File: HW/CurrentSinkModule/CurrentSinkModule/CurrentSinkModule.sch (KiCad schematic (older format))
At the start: 22 parts

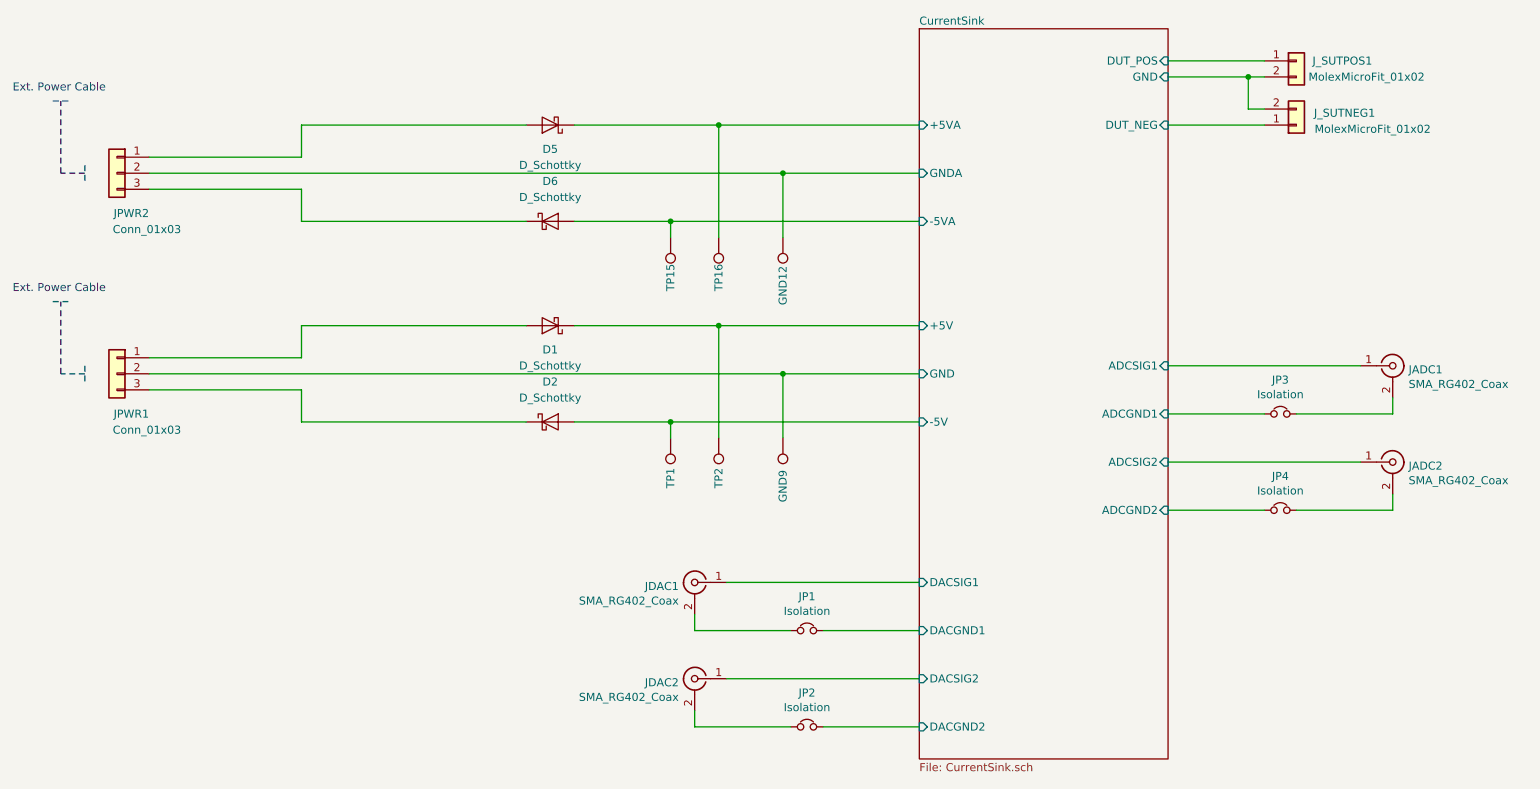
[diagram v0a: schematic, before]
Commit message: Finished CurrentSinkRevC layout
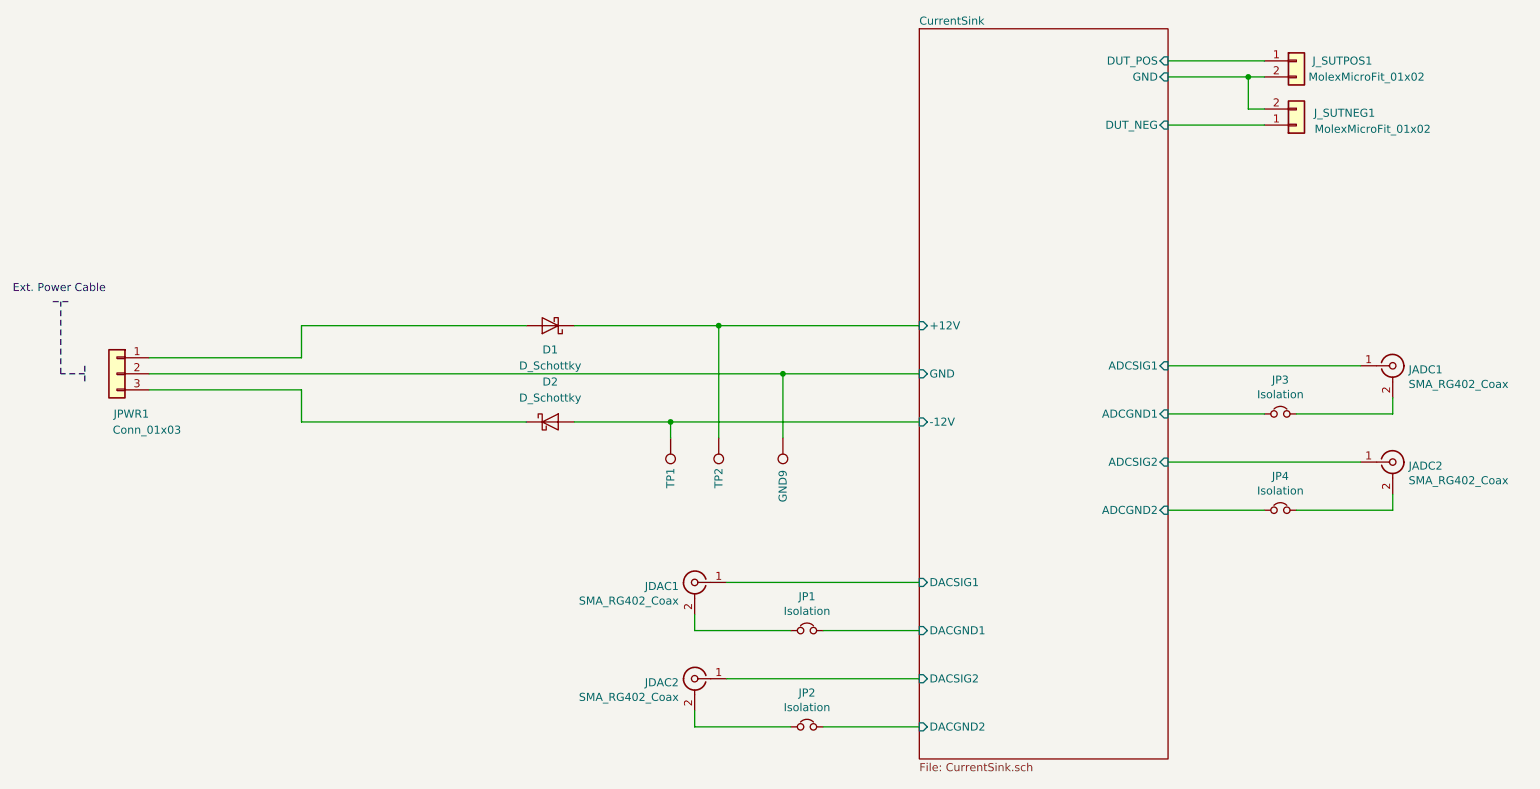
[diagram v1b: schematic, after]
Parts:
- removed D5, D6: D_Schottky, Diode_SMD:D_SOD-123, symbol Device:D_Schottky
- removed GND12, TP15, TP16: TestPoint, TestPoint:TestPoint_Pad_2.0x2.0mm, symbol Connector:TestPoint
- removed JPWR2: Conn_01x03, Connector_Molex:Molex_KK-254_AE-6410-03A_1x03_P2.54mm_Vertical, symbol Connector_Generic:Conn_01x03
- JP1, JP2, JP3, JP4: footprint Jumper:SolderJumper-2_P1.3mm_Bridged_Pad1.0x1.5mm -> Jumper:SolderJumper-2_P1.3mm_Open_Pad1.0x1.5mm
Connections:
- net CurrentSink/GND is gone; now on net CurrentSink/GND: J_SUTNEG1.2 (Pin_2), J_SUTPOS1.2 (Pin_2)
- net CurrentSink/GND: no longer GND9.1, JPWR1.2 (Pin_2)
- net CurrentSink/+5V renamed CurrentSink/+12V
- net CurrentSink/-5V renamed CurrentSink/-12V
- new net CurrentSink/GND: GND9.1, JPWR1.2 (Pin_2)
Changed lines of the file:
@@
 F 0 "JP1" H 5950 5562 50  0000 C CNN
 F 1 "Isolation" H 5950 5471 50  0000 C CNN
-F 2 "Jumper:SolderJumper-2_P1.3mm_Bridged_Pad1.0x1.5mm" H 5950 5350 50  0001 C CNN
+F 2 "Jumper:SolderJumper-2_P1.3mm_Open_Pad1.0x1.5mm" H 5950 5350 50  0001 C CNN
 F 3 "~" H 5950 5350 50  0001 C CNN
 	1    5950 5350
@@
 F 0 "JP2" H 5950 6162 50  0000 C CNN
 F 1 "Isolation" H 5950 6071 50  0000 C CNN
-F 2 "Jumper:SolderJumper-2_P1.3mm_Bridged_Pad1.0x1.5mm" H 5950 5950 50  0001 C CNN
+F 2 "Jumper:SolderJumper-2_P1.3mm_Open_Pad1.0x1.5mm" H 5950 5950 50  0001 C CNN
 F 3 "~" H 5950 5950 50  0001 C CNN
 	1    5950 5950
@@
 F 0 "JP3" H 8900 4212 50  0000 C CNN
 F 1 "Isolation" H 8900 4121 50  0000 C CNN
-F 2 "Jumper:SolderJumper-2_P1.3mm_Bridged_Pad1.0x1.5mm" H 8900 4000 50  0001 C CNN
+F 2 "Jumper:SolderJumper-2_P1.3mm_Open_Pad1.0x1.5mm" H 8900 4000 50  0001 C CNN
 F 3 "~" H 8900 4000 50  0001 C CNN
 	1    8900 4000
@@
 F 0 "JP4" H 8900 4812 50  0000 C CNN
 F 1 "Isolation" H 8900 4721 50  0000 C CNN
-F 2 "Jumper:SolderJumper-2_P1.3mm_Bridged_Pad1.0x1.5mm" H 8900 4600 50  0001 C CNN
+F 2 "Jumper:SolderJumper-2_P1.3mm_Open_Pad1.0x1.5mm" H 8900 4600 50  0001 C CNN
 F 3 "~" H 8900 4600 50  0001 C CNN
 	1    8900 4600
@@
 F12 "DACGND1" I L 6650 5350 50
 F13 "DACGND2" I L 6650 5950 50
-F14 "+5V" I L 6650 3450 50
-F15 "-5V" I L 6650 4050 50
-F16 "+5VA" I L 6650 2200 50
-F17 "-5VA" I L 6650 2800 50
-F18 "GNDA" I L 6650 2500 50
+F14 "+12V" I L 6650 3450 50
+F15 "-12V" I L 6650 4050 50
 $EndSheet
-Wire Wire Line
-	2800 2200 2800 2400
-$Comp
-L Connector_Generic:Conn_01x03 JPWR2
-U 1 1 5E00E9C0
-P 1650 2500
-F 0 "JPWR2" H 1450 2250 50  0000 L CNN
-F 1 "Conn_01x03" H 1250 2150 50  0000 L CNN
-F 2 "Connector_Molex:Molex_KK-254_AE-6410-03A_1x03_P2.54mm_Vertical" H 1650 2500 50  0001 C CNN
-F 3 "~" H 1650 2500 50  0001 C CNN
-	1    1650 2500
-	-1   0    0    -1
-$EndComp
-Wire Notes Line
-	1450 2500 1300 2500
-Wire Notes Line
-	1300 2500 1300 2050
-Wire Notes Line
-	1250 2050 1350 2050
-Wire Notes Line
-	1450 2450 1450 2550
-Text Notes 1000 2000 0    50   ~ 0
-Ext. Power Cable
-$Comp
-L Device:D_Schottky D5
-U 1 1 5E00E9CF
-P 4350 2200
-F 0 "D5" H 4350 2350 50  0000 C CNN
-F 1 "D_Schottky" H 4350 2450 50  0000 C CNN
-F 2 "Diode_SMD:D_SOD-123" H 4350 2200 50  0001 C CNN
-F 3 "~" H 4350 2200 50  0001 C CNN
-	1    4350 2200
-	-1   0    0    1
-$EndComp
-$Comp
-L Device:D_Schottky D6
-U 1 1 5E00E9D9
-P 4350 2800
-F 0 "D6" H 4350 3050 50  0000 C CNN
-F 1 "D_Schottky" H 4350 2950 50  0000 C CNN
-F 2 "Diode_SMD:D_SOD-123" H 4350 2800 50  0001 C CNN
-F 3 "~" H 4350 2800 50  0001 C CNN
-	1    4350 2800
-	1    0    0    -1
-$EndComp
-Wire Wire Line
-	4200 2200 2800 2200
-Wire Wire Line
-	4500 2800 5100 2800
-Wire Wire Line
-	4500 2200 5400 2200
-Wire Wire Line
-	5100 2900 5100 2800
-$Comp
-L Connector:TestPoint TP?
-U 1 1 5E00E9EA
-P 5100 2900
-AR Path="/5C977310/5E00E9EA" Ref="TP?"  Part="1"
-AR Path="/5E00E9EA" Ref="TP15"  Part="1"
-F 0 "TP15" V 5100 3150 50  0000 C CNN
-F 1 "TestPoint" V 5204 2974 50  0001 C CNN
-F 2 "TestPoint:TestPoint_Pad_2.0x2.0mm" H 5300 2900 50  0001 C CNN
-F 3 "https://cdn.harwin.com/pdfs/S2751R.pdf" H 5300 2900 50  0001 C CNN
-F 4 "855-S2751-46R" H 5100 2900 50  0001 C CNN "MouserNo"
-F 5 "S2751-46R" H 5100 2900 50  0001 C CNN "Mfr. No:"
-F 6 "Harwin" H 5100 2900 50  0001 C CNN "Mfr:"
-	1    5100 2900
-	-1   0    0    1
-$EndComp
-Wire Wire Line
-	5400 2900 5400 2200
-$Comp
-L Connector:TestPoint TP?
-U 1 1 5E00E9F8
-P 5400 2900
-AR Path="/5C977310/5E00E9F8" Ref="TP?"  Part="1"
-AR Path="/5E00E9F8" Ref="TP16"  Part="1"
-F 0 "TP16" V 5400 3150 50  0000 C CNN
-F 1 "TestPoint" V 5504 2974 50  0001 C CNN
-F 2 "TestPoint:TestPoint_Pad_2.0x2.0mm" H 5600 2900 50  0001 C CNN
-F 3 "https://cdn.harwin.com/pdfs/S2751R.pdf" H 5600 2900 50  0001 C CNN
-F 4 "855-S2751-46R" H 5400 2900 50  0001 C CNN "MouserNo"
-F 5 "S2751-46R" H 5400 2900 50  0001 C CNN "Mfr. No:"
-F 6 "Harwin" H 5400 2900 50  0001 C CNN "Mfr:"
-	1    5400 2900
-	-1   0    0    1
-$EndComp
-Connection ~ 5400 2200
-Connection ~ 5100 2800
-Wire Wire Line
-	1850 2600 2800 2600
-Wire Wire Line
-	2800 2800 2800 2600
-Wire Wire Line
-	2800 2800 4200 2800
-Wire Wire Line
-	5800 2900 5800 2500
-$Comp
-L Connector:TestPoint GND?
-U 1 1 5E00EA0B
-P 5800 2900
-AR Path="/5C977310/5E00EA0B" Ref="GND?"  Part="1"
-AR Path="/5E00EA0B" Ref="GND12"  Part="1"
-F 0 "GND12" V 5800 3200 50  0000 C CNN
-F 1 "TestPoint" V 5904 2974 50  0001 C CNN
-F 2 "TestPoint:TestPoint_Pad_2.0x2.0mm" H 6000 2900 50  0001 C CNN
-F 3 "https://cdn.harwin.com/pdfs/S2751R.pdf" H 6000 2900 50  0001 C CNN
-F 4 "855-S2751-46R" H 5800 2900 50  0001 C CNN "MouserNo"
-F 5 "S2751-46R" H 5800 2900 50  0001 C CNN "Mfr. No:"
-F 6 "Harwin" H 5800 2900 50  0001 C CNN "Mfr:"
-	1    5800 2900
-	-1   0    0    1
-$EndComp
-Connection ~ 5800 2500
-Wire Wire Line
-	1850 2500 5800 2500
-Wire Wire Line
-	2800 2400 1850 2400
-Wire Wire Line
-	5400 2200 6650 2200
-Wire Wire Line
-	5800 2500 6650 2500
-Wire Wire Line
-	5100 2800 6650 2800
 $EndSCHEMATC

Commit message: added 24V PSU
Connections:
- net CurrentSink/GND is gone; now on net CurrentSink/GND: J_SUTNEG1.2 (Pin_2), J_SUTPOS1.2 (Pin_2)
- net CurrentSink/GND: no longer GND9.1, JPWR1.2 (Pin_2)
- new net CurrentSink/GND: GND9.1, JPWR1.2 (Pin_2)
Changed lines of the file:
@@
 Rev "C"
 Comp "Designed by C Sutton"
-Comment1 ""
+Comment1 "Nominal Current Draw (0.1Ω Power Resistors): 95mA"
 Comment2 ""
 Comment3 ""
